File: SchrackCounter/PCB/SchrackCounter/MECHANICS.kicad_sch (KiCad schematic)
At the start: 24 parts, among them J3 Conn_01x02_Pin, J4 Conn_01x02_Pin, J5 MEM2067-02-180-00-A_REVB, M1 Fan_CPU_4pin, SW1 SW_Push, SW2 SW_Push, SW3 SW_Push, SW4 SW_Push

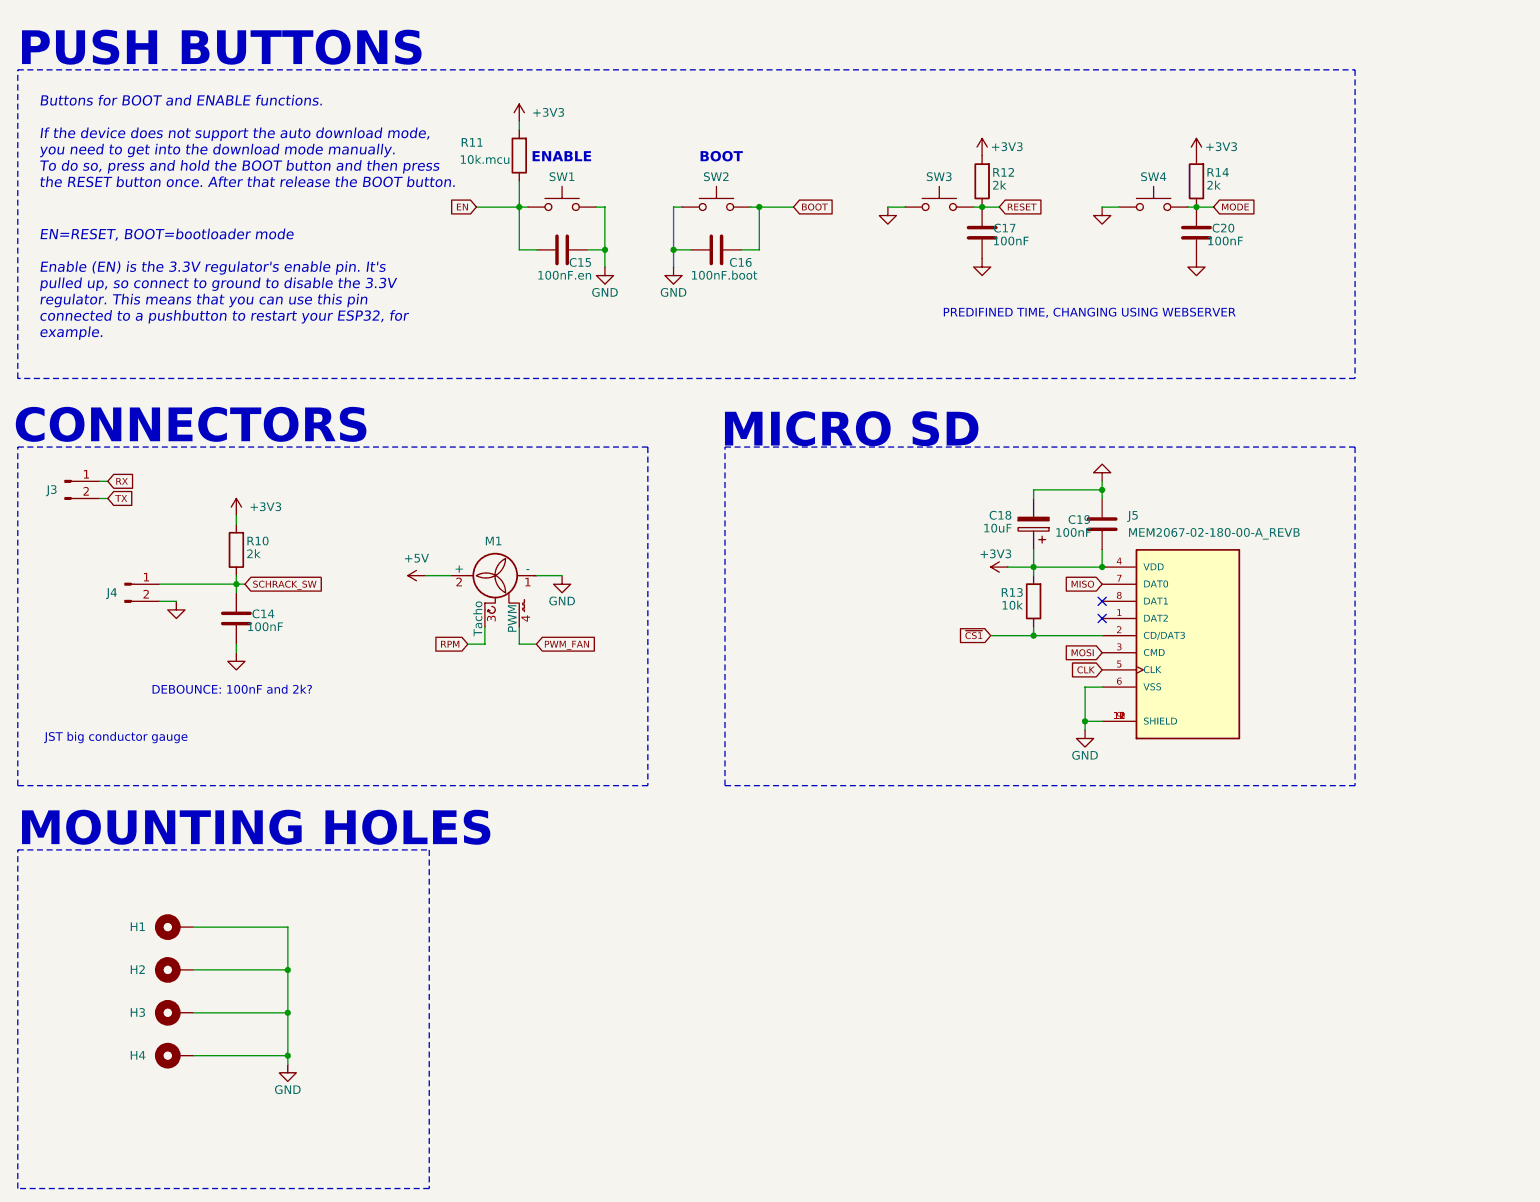
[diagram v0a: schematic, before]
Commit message: Schematic and PCB update
LDO Regulator, and some layout update
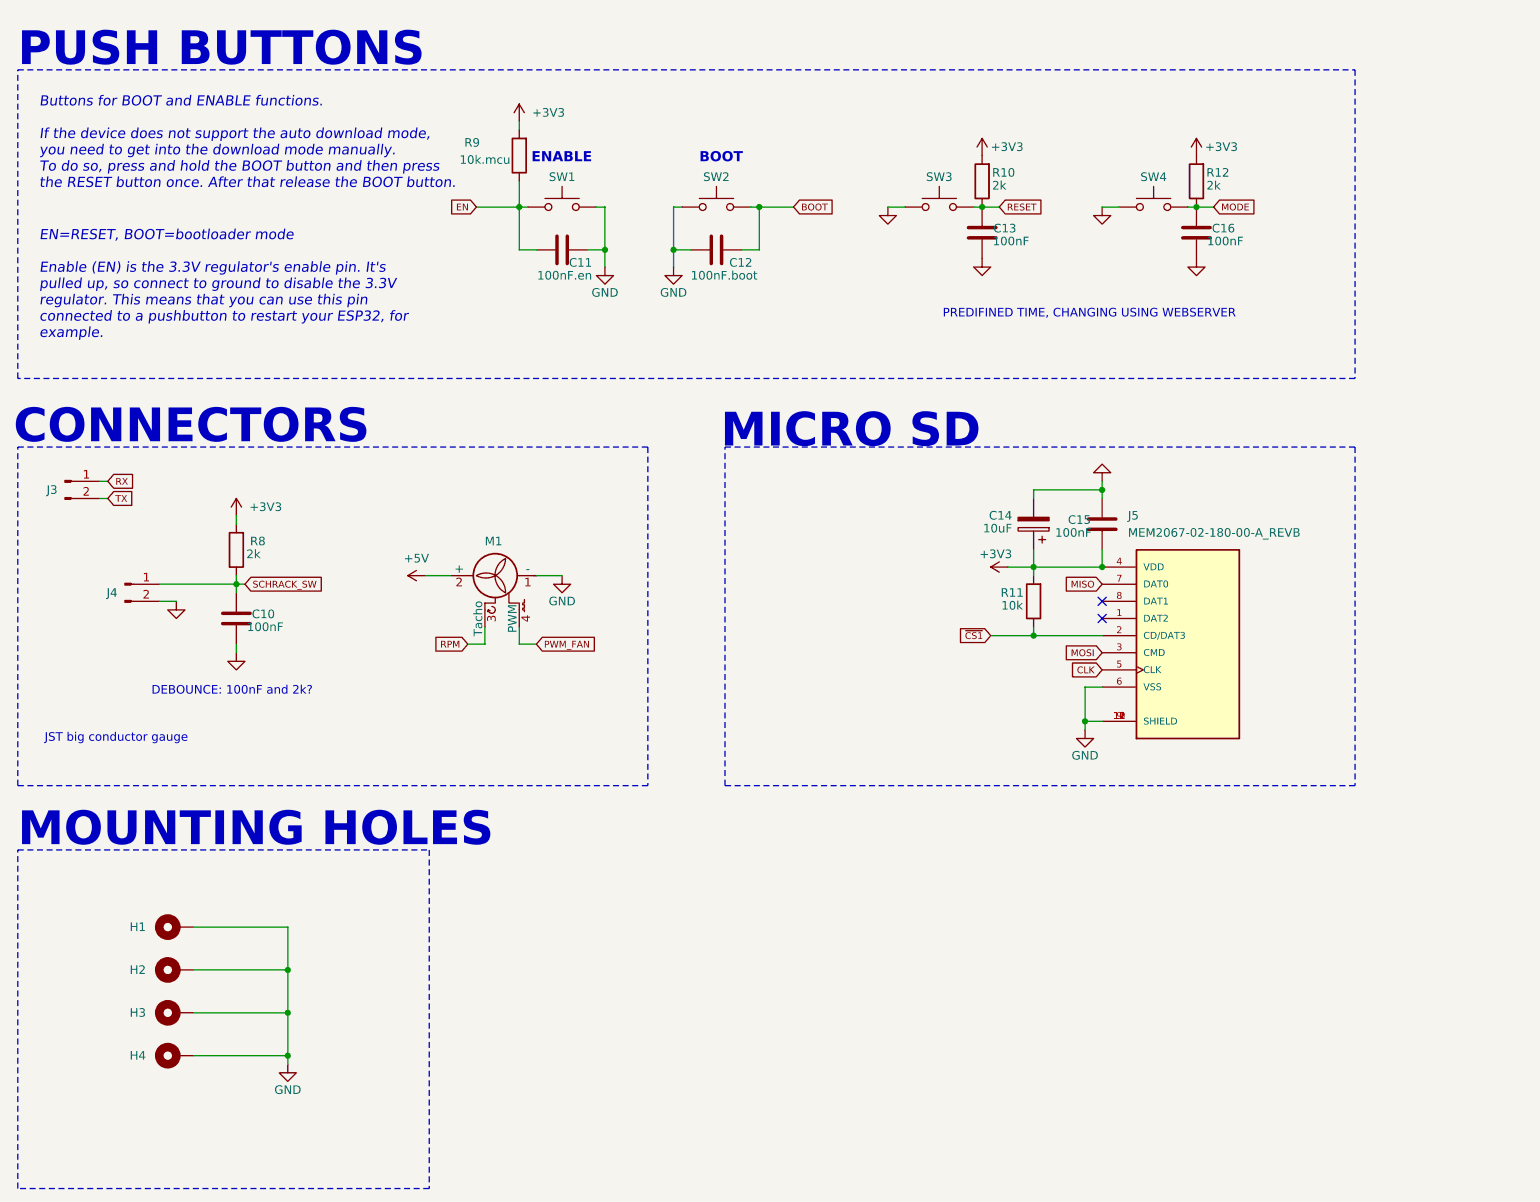
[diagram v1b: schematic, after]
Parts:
- renumbered C14 to C10, C15 to C11, C16 to C12, C17 to C13, C18 to C14, C19 to C15, C20 to C16, R12 to R10, R13 to R11, R14 to R12, R10 to R8, R11 to R9
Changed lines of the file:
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@@
 		(on_board yes)
 		(dnp no)
-		(property "Reference" "#PWR035"
+		(property "Reference" "#PWR029"
 			(at 114.3 36.83 0)
 			(effects
@@
 			(project "SchrackCounter"
 				(path "/d96f2ffc-3f4c-4f71-b693-29f6b8c3245d/0ccd8f36-c6f2-454f-91e2-c1976b699e0e"
-					(reference "#PWR035")
+					(reference "#PWR029")
 					(unit 1)
 				)
@@
 		(on_board yes)
 		(dnp no)
-		(property "Reference" "#PWR047"
+		(property "Reference" "#PWR041"
 			(at 214.63 59.69 0)
 			(effects
@@
 			(project "SchrackCounter"
 				(path "/d96f2ffc-3f4c-4f71-b693-29f6b8c3245d/0ccd8f36-c6f2-454f-91e2-c1976b699e0e"
-					(reference "#PWR047")
+					(reference "#PWR041")
 					(unit 1)
 				)
@@
 		(on_board yes)
 		(dnp no)
-		(property "Reference" "#PWR043"
+		(property "Reference" "#PWR037"
 			(at 198.12 129.54 0)
 			(effects
@@
 			(project "SchrackCounter"
 				(path "/d96f2ffc-3f4c-4f71-b693-29f6b8c3245d/0ccd8f36-c6f2-454f-91e2-c1976b699e0e"
-					(reference "#PWR043")
+					(reference "#PWR037")
 					(unit 1)
 				)
@@
 		(on_board yes)
 		(dnp no)
-		(property "Reference" "#PWR042"
+		(property "Reference" "#PWR036"
 			(at 190.5 99.06 0)
 			(effects
@@
 			(project "SchrackCounter"
 				(path "/d96f2ffc-3f4c-4f71-b693-29f6b8c3245d/0ccd8f36-c6f2-454f-91e2-c1976b699e0e"
-					(reference "#PWR042")
+					(reference "#PWR036")
 					(unit 1)
 				)
@@
 		(on_board yes)
 		(dnp no)
-		(property "Reference" "R10"
+		(property "Reference" "R8"
 			(at 75.565 95.25 0)
 			(effects
@@
 			(project "SchrackCounter"
 				(path "/d96f2ffc-3f4c-4f71-b693-29f6b8c3245d/0ccd8f36-c6f2-454f-91e2-c1976b699e0e"
-					(reference "R10")
+					(reference "R8")
 					(unit 1)
 				)
@@
 		(on_board yes)
 		(dnp no)
-		(property "Reference" "C18"
+		(property "Reference" "C14"
 			(at 187.325 91.44 0)
 			(effects
@@
 			(project "SchrackCounter"
 				(path "/d96f2ffc-3f4c-4f71-b693-29f6b8c3245d/0ccd8f36-c6f2-454f-91e2-c1976b699e0e"
-					(reference "C18")
+					(reference "C14")
 					(unit 1)
 				)
@@
 		(on_board yes)
 		(dnp no)
-		(property "Reference" "R12"
+		(property "Reference" "R10"
 			(at 186.055 40.64 0)
 			(effects
@@
 			(project "SchrackCounter"
 				(path "/d96f2ffc-3f4c-4f71-b693-29f6b8c3245d/0ccd8f36-c6f2-454f-91e2-c1976b699e0e"
-					(reference "R12")
+					(reference "R10")
 					(unit 1)
 				)
@@
 		(on_board yes)
 		(dnp no)
-		(property "Reference" "#PWR038"
+		(property "Reference" "#PWR032"
 			(at 137.16 60.96 0)
 			(effects
@@
 			(project "SchrackCounter"
 				(path "/d96f2ffc-3f4c-4f71-b693-29f6b8c3245d/0ccd8f36-c6f2-454f-91e2-c1976b699e0e"
-					(reference "#PWR038")
+					(reference "#PWR032")
 					(unit 1)
 				)
@@
 		(on_board yes)
 		(dnp no)
-		(property "Reference" "#PWR037"
+		(property "Reference" "#PWR031"
 			(at 127 60.96 0)
 			(effects
@@
 			(project "SchrackCounter"
 				(path "/d96f2ffc-3f4c-4f71-b693-29f6b8c3245d/0ccd8f36-c6f2-454f-91e2-c1976b699e0e"
-					(reference "#PWR037")
+					(reference "#PWR031")
 					(unit 1)
 				)
@@
 		(on_board yes)
 		(dnp no)
-		(property "Reference" "#PWR044"
+		(property "Reference" "#PWR038"
 			(at 200.66 52.07 0)
 			(effects
@@
 			(project "SchrackCounter"
 				(path "/d96f2ffc-3f4c-4f71-b693-29f6b8c3245d/0ccd8f36-c6f2-454f-91e2-c1976b699e0e"
-					(reference "#PWR044")
+					(reference "#PWR038")
 					(unit 1)
 				)
@@
 		(on_board yes)
 		(dnp no)
-		(property "Reference" "#PWR032"
+		(property "Reference" "#PWR025"
 			(at 72.39 95.25 0)
 			(effects
@@
 			(project "SchrackCounter"
 				(path "/d96f2ffc-3f4c-4f71-b693-29f6b8c3245d/0ccd8f36-c6f2-454f-91e2-c1976b699e0e"
-					(reference "#PWR032")
+					(reference "#PWR025")
 					(unit 1)
 				)
@@
 		(on_board yes)
 		(dnp no)
-		(property "Reference" "C17"
+		(property "Reference" "C13"
 			(at 187.96 48.895 0)
 			(effects
@@
 			(project "SchrackCounter"
 				(path "/d96f2ffc-3f4c-4f71-b693-29f6b8c3245d/0ccd8f36-c6f2-454f-91e2-c1976b699e0e"
-					(reference "C17")
+					(reference "C13")
 					(unit 1)
 				)
@@
 		(on_board yes)
 		(dnp no)
-		(property "Reference" "#PWR033"
+		(property "Reference" "#PWR026"
 			(at 72.39 118.11 0)
 			(effects
@@
 			(project "SchrackCounter"
 				(path "/d96f2ffc-3f4c-4f71-b693-29f6b8c3245d/0ccd8f36-c6f2-454f-91e2-c1976b699e0e"
-					(reference "#PWR033")
+					(reference "#PWR026")
 					(unit 1)
 				)
@@
 		(on_board yes)
 		(dnp no)
-		(property "Reference" "#PWR041"
+		(property "Reference" "#PWR035"
 			(at 182.88 59.69 0)
 			(effects
@@
 			(project "SchrackCounter"
 				(path "/d96f2ffc-3f4c-4f71-b693-29f6b8c3245d/0ccd8f36-c6f2-454f-91e2-c1976b699e0e"
-					(reference "#PWR041")
+					(reference "#PWR035")
 					(unit 1)
 				)
@@
 		(on_board yes)
 		(dnp no)
-		(property "Reference" "C19"
+		(property "Reference" "C15"
 			(at 195.58 92.075 0)
 			(effects
@@
 			(project "SchrackCounter"
 				(path "/d96f2ffc-3f4c-4f71-b693-29f6b8c3245d/0ccd8f36-c6f2-454f-91e2-c1976b699e0e"
-					(reference "C19")
+					(reference "C15")
 					(unit 1)
 				)
@@
 		(on_board yes)
 		(dnp no)
-		(property "Reference" "R11"
+		(property "Reference" "R9"
 			(at 107.315 36.195 0)
 			(effects
@@
 			(project "SchrackCounter"
 				(path "/d96f2ffc-3f4c-4f71-b693-29f6b8c3245d/0ccd8f36-c6f2-454f-91e2-c1976b699e0e"
-					(reference "R11")
+					(reference "R9")
 					(unit 1)
 				)
@@
 		(on_board yes)
 		(dnp no)
-		(property "Reference" "#PWR030"
+		(property "Reference" "#PWR024"
 			(at 63.5 110.49 0)
 			(effects
@@
 			(project "SchrackCounter"
 				(path "/d96f2ffc-3f4c-4f71-b693-29f6b8c3245d/0ccd8f36-c6f2-454f-91e2-c1976b699e0e"
-					(reference "#PWR030")
+					(reference "#PWR024")
 					(unit 1)
 				)
@@
 		(on_board yes)
 		(dnp no)
-		(property "Reference" "#PWR045"
+		(property "Reference" "#PWR039"
 			(at 200.66 80.01 0)
 			(effects
@@
 			(project "SchrackCounter"
 				(path "/d96f2ffc-3f4c-4f71-b693-29f6b8c3245d/0ccd8f36-c6f2-454f-91e2-c1976b699e0e"
-					(reference "#PWR045")
+					(reference "#PWR039")
 					(unit 1)
 				)
@@
 		(on_board yes)
 		(dnp no)
-		(property "Reference" "#PWR034"
+		(property "Reference" "#PWR028"
 			(at 104.14 100.33 0)
 			(effects
@@
 			(project ""
 				(path "/d96f2ffc-3f4c-4f71-b693-29f6b8c3245d/0ccd8f36-c6f2-454f-91e2-c1976b699e0e"
-					(reference "#PWR034")
+					(reference "#PWR028")
 					(unit 1)
 				)
@@
 		(on_board yes)
 		(dnp no)
-		(property "Reference" "#PWR031"
+		(property "Reference" "#PWR027"
 			(at 80.01 179.07 0)
 			(effects
@@
 			(project "SchrackCounter"
 				(path "/d96f2ffc-3f4c-4f71-b693-29f6b8c3245d/0ccd8f36-c6f2-454f-91e2-c1976b699e0e"
-					(reference "#PWR031")
+					(reference "#PWR027")
 					(unit 1)
 				)
@@
 		(on_board yes)
 		(dnp no)
-		(property "Reference" "R14"
+		(property "Reference" "R12"
 			(at 217.805 40.64 0)
 			(effects
@@
 			(project "SchrackCounter"
 				(path "/d96f2ffc-3f4c-4f71-b693-29f6b8c3245d/0ccd8f36-c6f2-454f-91e2-c1976b699e0e"
-					(reference "R14")
+					(reference "R12")
 					(unit 1)
 				)
@@
 		(on_board yes)
 		(dnp no)
-		(property "Reference" "#PWR036"
+		(property "Reference" "#PWR030"
 			(at 120.65 106.68 0)
 			(effects
@@
 			(project "SchrackCounter"
 				(path "/d96f2ffc-3f4c-4f71-b693-29f6b8c3245d/0ccd8f36-c6f2-454f-91e2-c1976b699e0e"
-					(reference "#PWR036")
+					(reference "#PWR030")
 					(unit 1)
 				)
@@
 		(on_board yes)
 		(dnp no)
-		(property "Reference" "#PWR040"
+		(property "Reference" "#PWR034"
 			(at 182.88 41.91 0)
 			(effects
@@
 			(project "SchrackCounter"
 				(path "/d96f2ffc-3f4c-4f71-b693-29f6b8c3245d/0ccd8f36-c6f2-454f-91e2-c1976b699e0e"
-					(reference "#PWR040")
+					(reference "#PWR034")
 					(unit 1)
 				)
@@
 		(on_board yes)
 		(dnp no)
-		(property "Reference" "C20"
+		(property "Reference" "C16"
 			(at 220.345 48.895 0)
 			(effects
@@
 			(project "SchrackCounter"
 				(path "/d96f2ffc-3f4c-4f71-b693-29f6b8c3245d/0ccd8f36-c6f2-454f-91e2-c1976b699e0e"
-					(reference "C20")
+					(reference "C16")
 					(unit 1)
 				)
@@
 		(on_board yes)
 		(dnp no)
-		(property "Reference" "#PWR039"
+		(property "Reference" "#PWR033"
 			(at 168.91 52.07 0)
 			(effects
@@
 			(project "SchrackCounter"
 				(path "/d96f2ffc-3f4c-4f71-b693-29f6b8c3245d/0ccd8f36-c6f2-454f-91e2-c1976b699e0e"
-					(reference "#PWR039")
+					(reference "#PWR033")
 					(unit 1)
 				)
@@
 		(on_board yes)
 		(dnp no)
-		(property "Reference" "R13"
+		(property "Reference" "R11"
 			(at 187.325 102.87 0)
 			(effects
@@
 			(project "SchrackCounter"
 				(path "/d96f2ffc-3f4c-4f71-b693-29f6b8c3245d/0ccd8f36-c6f2-454f-91e2-c1976b699e0e"
-					(reference "R13")
+					(reference "R11")
 					(unit 1)
 				)
@@
 		(on_board yes)
 		(dnp no)
-		(property "Reference" "#PWR046"
+		(property "Reference" "#PWR040"
 			(at 214.63 41.91 0)
 			(effects
@@
 			(project "SchrackCounter"
 				(path "/d96f2ffc-3f4c-4f71-b693-29f6b8c3245d/0ccd8f36-c6f2-454f-91e2-c1976b699e0e"
-					(reference "#PWR046")
+					(reference "#PWR040")
 					(unit 1)
 				)
@@
 		(on_board yes)
 		(dnp no)
-		(property "Reference" "C15"
+		(property "Reference" "C11"
 			(at 125.095 53.975 90)
 			(effects
@@
 			(project "SchrackCounter"
 				(path "/d96f2ffc-3f4c-4f71-b693-29f6b8c3245d/0ccd8f36-c6f2-454f-91e2-c1976b699e0e"
-					(reference "C15")
+					(reference "C11")
 					(unit 1)
 				)
@@
 		(on_board yes)
 		(dnp no)
-		(property "Reference" "C14"
+		(property "Reference" "C10"
 			(at 78.105 106.045 0)
 			(effects
@@
 			(project "SchrackCounter"
 				(path "/d96f2ffc-3f4c-4f71-b693-29f6b8c3245d/0ccd8f36-c6f2-454f-91e2-c1976b699e0e"
-					(reference "C14")
+					(reference "C10")
 					(unit 1)
 				)
@@
 		(on_board yes)
 		(dnp no)
-		(property "Reference" "C16"
+		(property "Reference" "C12"
 			(at 145.415 53.975 90)
 			(effects
@@
 			(project "SchrackCounter"
 				(path "/d96f2ffc-3f4c-4f71-b693-29f6b8c3245d/0ccd8f36-c6f2-454f-91e2-c1976b699e0e"
-					(reference "C16")
-					(unit 1)
-				)
+					(reference "C12")
+					(unit 1)
+				)
